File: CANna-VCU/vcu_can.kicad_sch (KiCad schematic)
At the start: 12 parts, among them U1 TCAN3400-Q1, U2 TCAN3400-Q1

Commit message: first draft of full board
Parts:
- removed C1, C2, C63, C64: 100n, Capacitor_SMD:C_0805_2012Metric_Pad1.18x1.45mm_HandSolder, symbol Device:C_Small
- removed C3, C65: 4.7n, Capacitor_SMD:C_0805_2012Metric_Pad1.18x1.45mm_HandSolder, symbol Device:C_Small
- removed R1, R10, R11, R2: 60R, Resistor_SMD:R_0805_2012Metric_Pad1.20x1.40mm_HandSolder, symbol Device:R_Small
- removed U1, U2: TCAN3400-Q1, Package_SO:SOIC-8_3.9x4.9mm_P1.27mm, symbol SUFST:TCAN34004-Q1
- added C53, C54: 100n, Capacitor_SMD:C_0402_1005Metric, symbol Device:C_Small
- added C55, C56: 4.7n, Capacitor_SMD:C_0402_1005Metric, symbol Device:C_Small
- added R88, R89, R90, R91: 60R, Resistor_SMD:R_0402_1005Metric, symbol Device:R_Small
- added U13, U14: LTC2875-DD, Package_DFN_QFN:DFN-8-1EP_3x3mm_P0.5mm_EP1.66x2.38mm, symbol Interface_CAN_LIN:LTC2875-DD
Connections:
- net +3V3: now also C53.2, C54.2, U13.3 (VCC), U14.3 (VCC)
- net GND: now also C53.1, C54.1, C55.2, C56.2, U13.2 (GND), U13.8 (RS), U13.9 (GND), U14.2 (GND), U14.8 (RS), U14.9 (GND)
- new net: C56.1, R90.1, R91.2, U14.5 (SPLIT)
- new net: C55.1, R88.1, R89.2, U13.5 (SPLIT)
- new net 0_CANH: R88.2, U13.7 (CANH)
- new net 0_CANL: R89.1, U13.6 (CANL)
- new net 1_CANH: R90.2, U14.7 (CANH)
- new net 1_CANL: R91.1, U14.6 (CANL)
- new net CAN0_RX: U13.4 (RXD)
- new net CAN0_TX: U13.1 (TXD)
- new net CAN1_RX: U14.4 (RXD)
- new net CAN1_TX: U14.1 (TXD)
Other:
- note added: "TODO - add tvs? - add choke? - add notes - add rs232 tranciver - add some way of setting termination easily - formatting - notes"

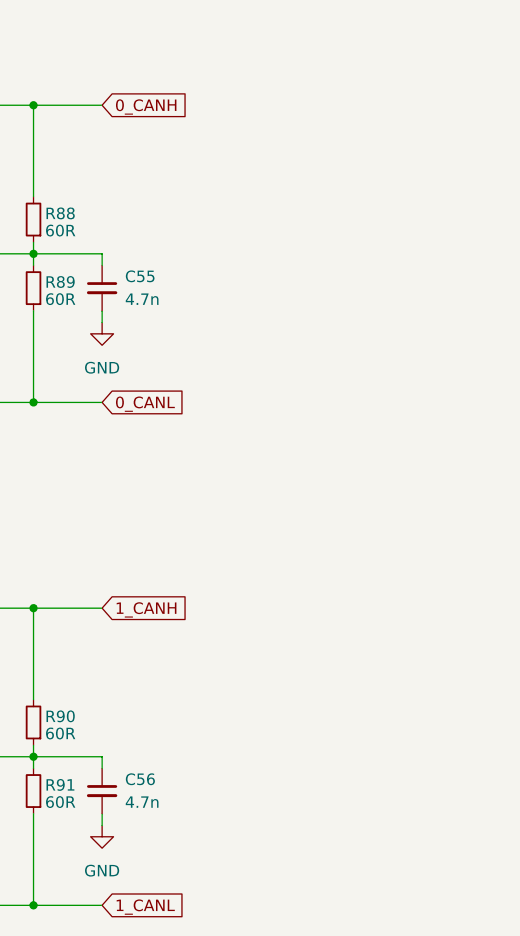
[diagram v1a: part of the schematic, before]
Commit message: added power managment bits
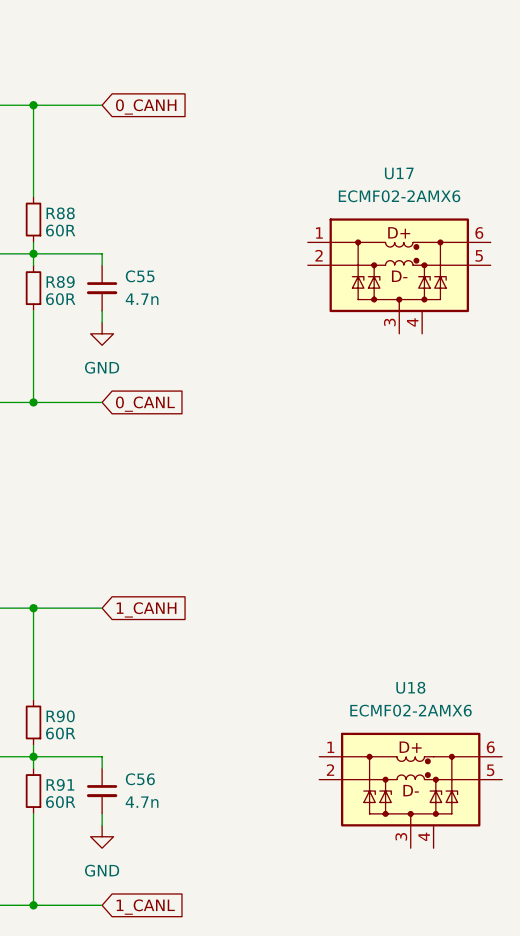
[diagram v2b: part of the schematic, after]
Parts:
- added U17, U18: ECMF02-2AMX6, Package_DFN_QFN:ST_UQFN-6L_1.5x1.7mm_P0.5mm, symbol Power_Protection:ECMF02-2AMX6
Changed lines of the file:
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@@
+	)
+	(symbol
+		(lib_id "Power_Protection:ECMF02-2AMX6")
+		(at 210.82 64.77 0)
+		(unit 1)
+		(exclude_from_sim no)
+		(in_bom yes)
+		(on_board yes)
+		(dnp no)
+		(fields_autoplaced yes)
+		(property "Reference" "U17"
+			(at 210.82 54.61 0)
+			(effects
+				(font
+					(size 1.27 1.27)
+				)
+			)
+		)
+		(property "Value" "ECMF02-2AMX6"
+			(at 210.82 57.15 0)
+			(effects
+				(font
+					(size 1.27 1.27)
+				)
+			)
+		)
+		(property "Footprint" "Package_DFN_QFN:ST_UQFN-6L_1.5x1.7mm_P0.5mm"
+			(at 210.82 85.09 0)
+			(effects
+				(font
+					(size 1.27 1.27)
+				)
+				(hide yes)
+			)
+		)
+		(property "Datasheet" "https://www.st.com/resource/en/datasheet/ecmf02-2amx6.pdf"
+			(at 210.82 87.63 0)
+			(effects
+				(font
+					(size 1.27 1.27)
+				)
+				(hide yes)
+			)
+		)
+		(property "Description" "Single Pair Common Mode Filter with ESD Protection, UQFN-6L"
+			(at 210.82 64.77 0)
+			(effects
+				(font
+					(size 1.27 1.27)
+				)
+				(hide yes)
+			)
+		)
+		(pin "2"
+		)
+		(pin "1"
+		)
+		(pin "3"
+		)
+		(pin "4"
+		)
+		(pin "6"
+		)
+		(pin "5"
+		)
+		(instances
+			(project "CANna-VCU"
+				(path "/d2b041cf-e68d-49d7-b31d-fe6ebce83d7e/e20bcd50-e953-4e5c-b1c5-a9c9ec609e53"
+					(reference "U17")
+					(unit 1)
+				)
+			)
+		)
 	)
 	(symbol
@@
 					(unit 1)
 				)
+			)
+		)
+	)
+	(symbol
+		(lib_id "Power_Protection:ECMF02-2AMX6")
+		(at 212.09 121.92 0)
+		(unit 1)
+		(exclude_from_sim no)
+		(in_bom yes)
+		(on_board yes)
+		(dnp no)
+		(fields_autoplaced yes)
+		(property "Reference" "U18"
+			(at 212.09 111.76 0)
+			(effects
+				(font
+					(size 1.27 1.27)
+				)
+			)
+		)
+		(property "Value" "ECMF02-2AMX6"
+			(at 212.09 114.3 0)
+			(effects
+				(font
+					(size 1.27 1.27)
+				)
+			)
+		)
+		(property "Footprint" "Package_DFN_QFN:ST_UQFN-6L_1.5x1.7mm_P0.5mm"
+			(at 212.09 142.24 0)
+			(effects
+				(font
+					(size 1.27 1.27)
+				)
+				(hide yes)
+			)
+		)
+		(property "Datasheet" "https://www.st.com/resource/en/datasheet/ecmf02-2amx6.pdf"
+			(at 212.09 144.78 0)
+			(effects
+				(font
+					(size 1.27 1.27)
+				)
+				(hide yes)
+			)
+		)
+		(property "Description" "Single Pair Common Mode Filter with ESD Protection, UQFN-6L"
+			(at 212.09 121.92 0)
+			(effects
+				(font
+					(size 1.27 1.27)
+				)
+				(hide yes)
+			)
+		)
+		(pin "2"
+		)
+		(pin "1"
+		)
+		(pin "3"
+		)
+		(pin "4"
+		)
+		(pin "6"
+		)
+		(pin "5"
+		)
+		(instances
+			(project "CANna-VCU"
+				(path "/d2b041cf-e68d-49d7-b31d-fe6ebce83d7e/e20bcd50-e953-4e5c-b1c5-a9c9ec609e53"
+					(reference "U18")
+					(unit 1)
+				)
